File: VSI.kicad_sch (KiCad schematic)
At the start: 30 parts, among them Q1 FGH40T120SMD, Q2 FGH40T120SMD, Q3 FGH40T120SMD, Q4 FGH40T120SMD, Q5 FGH40T120SMD, Q6 FGH40T120SMD

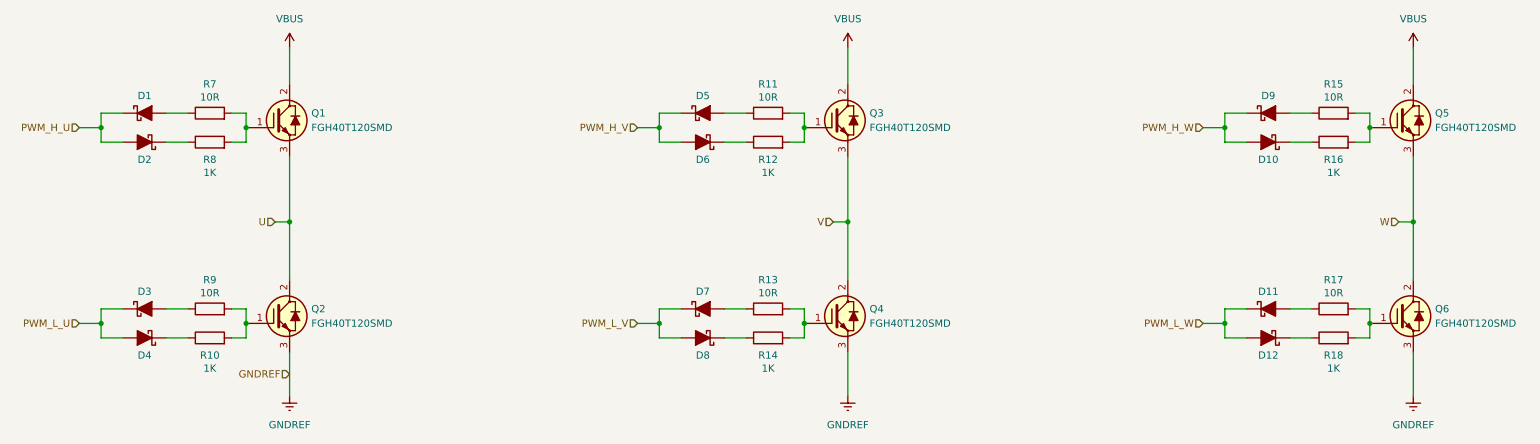
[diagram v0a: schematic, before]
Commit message: added local lib as module
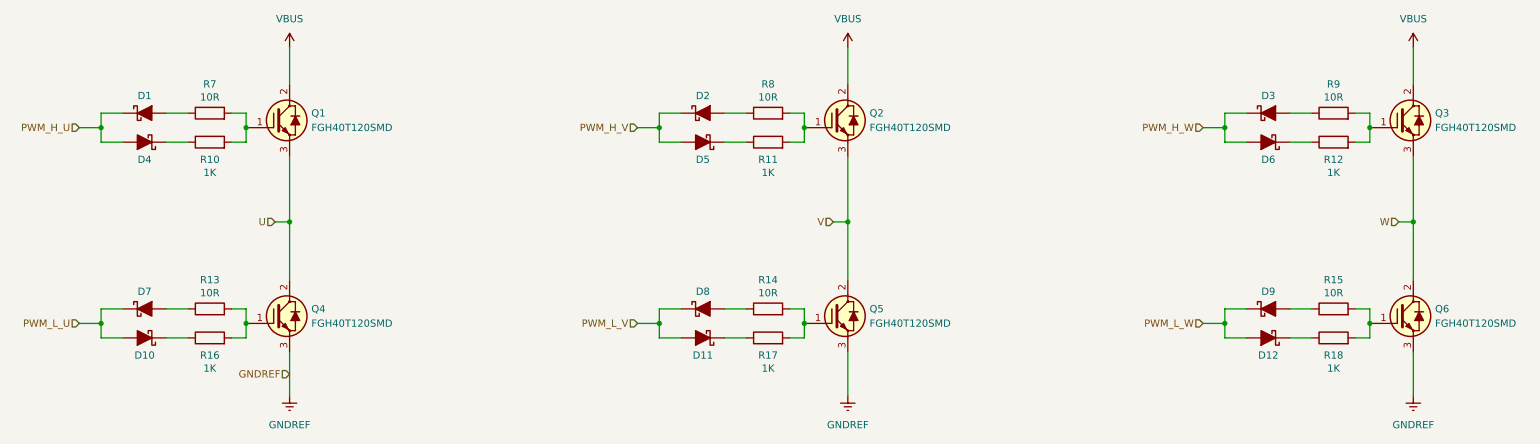
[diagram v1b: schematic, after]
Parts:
- renumbered D4 to D10, D8 to D11, D5 to D2, D9 to D3, D2 to D4, D6 to D5, D10 to D6, D3 to D7, D7 to D8, D11 to D9, Q3 to Q2, Q5 to Q3, Q2 to Q4, Q4 to Q5, R8 to R10, R12 to R11, R16 to R12, R9 to R13, R13 to R14, R17 to R15, R10 to R16, R14 to R17, R11 to R8, R15 to R9
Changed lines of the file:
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@@
 		(on_board yes)
 		(dnp no)
-		(property "Reference" "D11"
+		(property "Reference" "D9"
 			(at 236.22 112.522 0)
 			(effects
@@
 			(project "inverter"
 				(path "/6a7e1a19-486b-4340-90f8-1e7274261ff8/7fd06deb-165d-4c78-9f28-893d6b6500d1"
-					(reference "D11")
+					(reference "D9")
 					(unit 1)
 				)
@@
 		(dnp no)
 		(fields_autoplaced yes)
-		(property "Reference" "#PWR04"
+		(property "Reference" "#PWR05"
 			(at 261.62 73.66 0)
 			(effects
@@
 			(project "inverter"
 				(path "/6a7e1a19-486b-4340-90f8-1e7274261ff8/7fd06deb-165d-4c78-9f28-893d6b6500d1"
-					(reference "#PWR04")
+					(reference "#PWR05")
 					(unit 1)
 				)
@@
 		(on_board yes)
 		(dnp no)
-		(property "Reference" "R12"
+		(property "Reference" "R11"
 			(at 148.59 89.408 90)
 			(effects
@@
 			(project "inverter"
 				(path "/6a7e1a19-486b-4340-90f8-1e7274261ff8/7fd06deb-165d-4c78-9f28-893d6b6500d1"
-					(reference "R12")
+					(reference "R11")
 					(unit 1)
 				)
@@
 		(on_board yes)
 		(dnp no)
-		(property "Reference" "R10"
+		(property "Reference" "R16"
 			(at 50.8 123.698 90)
 			(effects
@@
 			(project "inverter"
 				(path "/6a7e1a19-486b-4340-90f8-1e7274261ff8/7fd06deb-165d-4c78-9f28-893d6b6500d1"
-					(reference "R10")
+					(reference "R16")
 					(unit 1)
 				)
@@
 		(dnp no)
 		(fields_autoplaced yes)
-		(property "Reference" "#PWR06"
+		(property "Reference" "#PWR07"
 			(at 162.56 137.16 0)
 			(effects
@@
 			(project "inverter"
 				(path "/6a7e1a19-486b-4340-90f8-1e7274261ff8/7fd06deb-165d-4c78-9f28-893d6b6500d1"
-					(reference "#PWR06")
+					(reference "#PWR07")
 					(unit 1)
 				)
@@
 		(on_board yes)
 		(dnp no)
-		(property "Reference" "R16"
+		(property "Reference" "R12"
 			(at 247.65 89.408 90)
 			(effects
@@
 			(project "inverter"
 				(path "/6a7e1a19-486b-4340-90f8-1e7274261ff8/7fd06deb-165d-4c78-9f28-893d6b6500d1"
-					(reference "R16")
+					(reference "R12")
 					(unit 1)
 				)
@@
 		(dnp no)
 		(fields_autoplaced yes)
-		(property "Reference" "Q5"
+		(property "Reference" "Q3"
 			(at 265.43 81.2799 0)
 			(effects
@@
 			(project "inverter"
 				(path "/6a7e1a19-486b-4340-90f8-1e7274261ff8/7fd06deb-165d-4c78-9f28-893d6b6500d1"
-					(reference "Q5")
+					(reference "Q3")
 					(unit 1)
 				)
@@
 		(dnp no)
 		(fields_autoplaced yes)
-		(property "Reference" "#PWR03"
+		(property "Reference" "#PWR04"
 			(at 162.56 73.66 0)
 			(effects
@@
 			(project "inverter"
 				(path "/6a7e1a19-486b-4340-90f8-1e7274261ff8/7fd06deb-165d-4c78-9f28-893d6b6500d1"
-					(reference "#PWR03")
+					(reference "#PWR04")
 					(unit 1)
 				)
@@
 		(on_board yes)
 		(dnp no)
-		(property "Reference" "R14"
+		(property "Reference" "R17"
 			(at 148.59 123.698 90)
 			(effects
@@
 			(project "inverter"
 				(path "/6a7e1a19-486b-4340-90f8-1e7274261ff8/7fd06deb-165d-4c78-9f28-893d6b6500d1"
-					(reference "R14")
+					(reference "R17")
 					(unit 1)
 				)
@@
 		(on_board yes)
 		(dnp no)
-		(property "Reference" "R9"
+		(property "Reference" "R13"
 			(at 50.8 110.49 90)
 			(effects
@@
 			(project "inverter"
 				(path "/6a7e1a19-486b-4340-90f8-1e7274261ff8/7fd06deb-165d-4c78-9f28-893d6b6500d1"
-					(reference "R9")
+					(reference "R13")
 					(unit 1)
 				)
@@
 		(on_board yes)
 		(dnp no)
-		(property "Reference" "D8"
+		(property "Reference" "D11"
 			(at 137.16 123.698 0)
 			(effects
@@
 			(project "inverter"
 				(path "/6a7e1a19-486b-4340-90f8-1e7274261ff8/7fd06deb-165d-4c78-9f28-893d6b6500d1"
-					(reference "D8")
+					(reference "D11")
 					(unit 1)
 				)
@@
 		(on_board yes)
 		(dnp no)
-		(property "Reference" "D6"
+		(property "Reference" "D5"
 			(at 137.16 89.408 0)
 			(effects
@@
 			(project "inverter"
 				(path "/6a7e1a19-486b-4340-90f8-1e7274261ff8/7fd06deb-165d-4c78-9f28-893d6b6500d1"
-					(reference "D6")
+					(reference "D5")
 					(unit 1)
 				)
@@
 		(dnp no)
 		(fields_autoplaced yes)
-		(property "Reference" "Q3"
+		(property "Reference" "Q2"
 			(at 166.37 81.2799 0)
 			(effects
@@
 			(project "inverter"
 				(path "/6a7e1a19-486b-4340-90f8-1e7274261ff8/7fd06deb-165d-4c78-9f28-893d6b6500d1"
-					(reference "Q3")
+					(reference "Q2")
 					(unit 1)
 				)
@@
 		(on_board yes)
 		(dnp no)
-		(property "Reference" "R17"
+		(property "Reference" "R15"
 			(at 247.65 110.49 90)
 			(effects
@@
 			(project "inverter"
 				(path "/6a7e1a19-486b-4340-90f8-1e7274261ff8/7fd06deb-165d-4c78-9f28-893d6b6500d1"
-					(reference "R17")
+					(reference "R15")
 					(unit 1)
 				)
@@
 		(on_board yes)
 		(dnp no)
-		(property "Reference" "R11"
+		(property "Reference" "R8"
 			(at 148.59 76.2 90)
 			(effects
@@
 			(project "inverter"
 				(path "/6a7e1a19-486b-4340-90f8-1e7274261ff8/7fd06deb-165d-4c78-9f28-893d6b6500d1"
-					(reference "R11")
+					(reference "R8")
 					(unit 1)
 				)
@@
 		(on_board yes)
 		(dnp no)
-		(property "Reference" "D10"
+		(property "Reference" "D6"
 			(at 236.22 89.408 0)
 			(effects
@@
 			(project "inverter"
 				(path "/6a7e1a19-486b-4340-90f8-1e7274261ff8/7fd06deb-165d-4c78-9f28-893d6b6500d1"
-					(reference "D10")
+					(reference "D6")
 					(unit 1)
 				)
@@
 		(on_board yes)
 		(dnp no)
-		(property "Reference" "D5"
+		(property "Reference" "D2"
 			(at 137.16 78.232 0)
 			(effects
@@
 			(project "inverter"
 				(path "/6a7e1a19-486b-4340-90f8-1e7274261ff8/7fd06deb-165d-4c78-9f28-893d6b6500d1"
-					(reference "D5")
+					(reference "D2")
 					(unit 1)
 				)
@@
 		(on_board yes)
 		(dnp no)
-		(property "Reference" "R15"
+		(property "Reference" "R9"
 			(at 247.65 76.2 90)
 			(effects
@@
 			(project "inverter"
 				(path "/6a7e1a19-486b-4340-90f8-1e7274261ff8/7fd06deb-165d-4c78-9f28-893d6b6500d1"
-					(reference "R15")
+					(reference "R9")
 					(unit 1)
 				)
@@
 		(on_board yes)
 		(dnp no)
-		(property "Reference" "D9"
+		(property "Reference" "D3"
 			(at 236.22 78.232 0)
 			(effects
@@
 			(project "inverter"
 				(path "/6a7e1a19-486b-4340-90f8-1e7274261ff8/7fd06deb-165d-4c78-9f28-893d6b6500d1"
-					(reference "D9")
+					(reference "D3")
 					(unit 1)
 				)
@@
 		(on_board yes)
 		(dnp no)
-		(property "Reference" "D7"
+		(property "Reference" "D8"
 			(at 137.16 112.522 0)
 			(effects
@@
 			(project "inverter"
 				(path "/6a7e1a19-486b-4340-90f8-1e7274261ff8/7fd06deb-165d-4c78-9f28-893d6b6500d1"
-					(reference "D7")
+					(reference "D8")
 					(unit 1)
 				)
@@
 		(on_board yes)
 		(dnp no)
-		(property "Reference" "D3"
+		(property "Reference" "D7"
 			(at 39.37 112.522 0)
 			(effects
@@
 			(project "inverter"
 				(path "/6a7e1a19-486b-4340-90f8-1e7274261ff8/7fd06deb-165d-4c78-9f28-893d6b6500d1"
-					(reference "D3")
+					(reference "D7")
 					(unit 1)
 				)
@@
 		(dnp no)
 		(fields_autoplaced yes)
-		(property "Reference" "#PWR02"
+		(property "Reference" "#PWR03"
 			(at 64.77 73.66 0)
 			(effects
@@
 			(project ""
 				(path "/6a7e1a19-486b-4340-90f8-1e7274261ff8/7fd06deb-165d-4c78-9f28-893d6b6500d1"
-					(reference "#PWR02")
+					(reference "#PWR03")
 					(unit 1)
 				)
@@
 		(dnp no)
 		(fields_autoplaced yes)
-		(property "Reference" "#PWR07"
+		(property "Reference" "#PWR08"
 			(at 261.62 137.16 0)
 			(effects
@@
 			(project "inverter"
 				(path "/6a7e1a19-486b-4340-90f8-1e7274261ff8/7fd06deb-165d-4c78-9f28-893d6b6500d1"
-					(reference "#PWR07")
+					(reference "#PWR08")
 					(unit 1)
 				)
@@
 		(dnp no)
 		(fields_autoplaced yes)
-		(property "Reference" "Q2"
+		(property "Reference" "Q4"
 			(at 68.58 115.5699 0)
 			(effects
@@
 			(project "inverter"
 				(path "/6a7e1a19-486b-4340-90f8-1e7274261ff8/7fd06deb-165d-4c78-9f28-893d6b6500d1"
-					(reference "Q2")
+					(reference "Q4")
 					(unit 1)
 				)
@@
 		(dnp no)
 		(fields_autoplaced yes)
-		(property "Reference" "Q4"
+		(property "Reference" "Q5"
 			(at 166.37 115.5699 0)
 			(effects
@@
 			(project "inverter"
 				(path "/6a7e1a19-486b-4340-90f8-1e7274261ff8/7fd06deb-165d-4c78-9f28-893d6b6500d1"
-					(reference "Q4")
+					(reference "Q5")
 					(unit 1)
 				)
@@
 		(on_board yes)
 		(dnp no)
-		(property "Reference" "D2"
+		(property "Reference" "D4"
 			(at 39.37 89.408 0)
 			(effects
@@
 			(project "inverter"
 				(path "/6a7e1a19-486b-4340-90f8-1e7274261ff8/7fd06deb-165d-4c78-9f28-893d6b6500d1"
-					(reference "D2")
+					(reference "D4")
 					(unit 1)
 				)
@@
 		(on_board yes)
 		(dnp no)
-		(property "Reference" "R8"
+		(property "Reference" "R10"
 			(at 50.8 89.408 90)
 			(effects
@@
 			(project "inverter"
 				(path "/6a7e1a19-486b-4340-90f8-1e7274261ff8/7fd06deb-165d-4c78-9f28-893d6b6500d1"
-					(reference "R8")
+					(reference "R10")
 					(unit 1)
 				)
@@
 		(on_board yes)
 		(dnp no)
-		(property "Reference" "R13"
+		(property "Reference" "R14"
 			(at 148.59 110.49 90)
 			(effects
@@
 			(project "inverter"
 				(path "/6a7e1a19-486b-4340-90f8-1e7274261ff8/7fd06deb-165d-4c78-9f28-893d6b6500d1"
-					(reference "R13")
+					(reference "R14")
 					(unit 1)
 				)
@@
 		(on_board yes)
 		(dnp no)
-		(property "Reference" "D4"
+		(property "Reference" "D10"
 			(at 39.37 123.698 0)
 			(effects
@@
 			(project "inverter"
 				(path "/6a7e1a19-486b-4340-90f8-1e7274261ff8/7fd06deb-165d-4c78-9f28-893d6b6500d1"
-					(reference "D4")
+					(reference "D10")
 					(unit 1)
 				)
@@
 		(dnp no)
 		(fields_autoplaced yes)
-		(property "Reference" "#PWR05"
+		(property "Reference" "#PWR06"
 			(at 64.77 137.16 0)
 			(effects
@@
 			(project ""
 				(path "/6a7e1a19-486b-4340-90f8-1e7274261ff8/7fd06deb-165d-4c78-9f28-893d6b6500d1"
-					(reference "#PWR05")
-					(unit 1)
-				)
+					(reference "#PWR06")
+					(unit 1)
+				)

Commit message: dev: added NC flags and fixed ERC warnings. Added custom design rules for PCB Design.
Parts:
- D1, D10, D11, D12, D2, D3, D4, D5, D6, D7, D8, D9: footprint (none) -> Diode_SMD:D_SOD-123
- R10, R11, R12, R13, R14, R15, R16, R17, R18, R7, R8, R9: footprint (none) -> Resistor_SMD:R_0805_2012Metric_Pad1.20x1.40mm_HandSolder
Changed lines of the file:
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@@
 			)
 		)
-		(property "Footprint" ""
+		(property "Footprint" "Diode_SMD:D_SOD-123"
 			(at 236.22 115.57 0)
 			(effects
@@
 			)
 		)
-		(property "Footprint" ""
+		(property "Footprint" "Resistor_SMD:R_0805_2012Metric_Pad1.20x1.40mm_HandSolder"
 			(at 148.59 88.138 90)
 			(effects
@@
 			)
 		)
-		(property "Footprint" ""
+		(property "Footprint" "Resistor_SMD:R_0805_2012Metric_Pad1.20x1.40mm_HandSolder"
 			(at 50.8 122.428 90)
 			(effects
@@
 			)
 		)
-		(property "Footprint" ""
+		(property "Footprint" "Resistor_SMD:R_0805_2012Metric_Pad1.20x1.40mm_HandSolder"
 			(at 247.65 88.138 90)
 			(effects
@@
 			)
 		)
-		(property "Footprint" ""
+		(property "Footprint" "Resistor_SMD:R_0805_2012Metric_Pad1.20x1.40mm_HandSolder"
 			(at 247.65 122.428 90)
 			(effects
@@
 			)
 		)
-		(property "Footprint" ""
+		(property "Footprint" "Resistor_SMD:R_0805_2012Metric_Pad1.20x1.40mm_HandSolder"
 			(at 148.59 122.428 90)
 			(effects
@@
 			)
 		)
-		(property "Footprint" ""
+		(property "Footprint" "Resistor_SMD:R_0805_2012Metric_Pad1.20x1.40mm_HandSolder"
 			(at 50.8 117.348 90)
 			(effects
@@
 			)
 		)
-		(property "Footprint" ""
+		(property "Footprint" "Diode_SMD:D_SOD-123"
 			(at 137.16 120.65 0)
 			(effects
@@
 			)
 		)
-		(property "Footprint" ""
+		(property "Footprint" "Diode_SMD:D_SOD-123"
 			(at 39.37 81.28 0)
 			(effects
@@
 			)
 		)
-		(property "Footprint" ""
+		(property "Footprint" "Resistor_SMD:R_0805_2012Metric_Pad1.20x1.40mm_HandSolder"
 			(at 50.8 83.058 90)
 			(effects
@@
 			)
 		)
-		(property "Footprint" ""
+		(property "Footprint" "Diode_SMD:D_SOD-123"
 			(at 236.22 120.65 0)
 			(effects
@@
 			)
 		)
-		(property "Footprint" ""
+		(property "Footprint" "Diode_SMD:D_SOD-123"
 			(at 137.16 86.36 0)
 			(effects
@@
 			)
 		)
-		(property "Footprint" ""
+		(property "Footprint" "Resistor_SMD:R_0805_2012Metric_Pad1.20x1.40mm_HandSolder"
 			(at 247.65 117.348 90)
 			(effects
@@
 			)
 		)
-		(property "Footprint" ""
+		(property "Footprint" "Resistor_SMD:R_0805_2012Metric_Pad1.20x1.40mm_HandSolder"
 			(at 148.59 83.058 90)
 			(effects
@@
 			)
 		)
-		(property "Footprint" ""
+		(property "Footprint" "Diode_SMD:D_SOD-123"
 			(at 236.22 86.36 0)
 			(effects
@@
 			)
 		)
-		(property "Footprint" ""
+		(property "Footprint" "Diode_SMD:D_SOD-123"
 			(at 137.16 81.28 0)
 			(effects
@@
 			)
 		)
-		(property "Footprint" ""
+		(property "Footprint" "Resistor_SMD:R_0805_2012Metric_Pad1.20x1.40mm_HandSolder"
 			(at 247.65 83.058 90)
 			(effects
@@
 			)
 		)
-		(property "Footprint" ""
+		(property "Footprint" "Diode_SMD:D_SOD-123"
 			(at 236.22 81.28 0)
 			(effects
@@
 			)
 		)
-		(property "Footprint" ""
+		(property "Footprint" "Diode_SMD:D_SOD-123"
 			(at 137.16 115.57 0)
 			(effects
@@
 			)
 		)
-		(property "Footprint" ""
+		(property "Footprint" "Diode_SMD:D_SOD-123"
 			(at 39.37 115.57 0)
 			(effects
@@
 			)
 		)
-		(property "Footprint" ""
+		(property "Footprint" "Diode_SMD:D_SOD-123"
 			(at 39.37 86.36 0)
 			(effects
@@
 			)
 		)
-		(property "Footprint" ""
+		(property "Footprint" "Resistor_SMD:R_0805_2012Metric_Pad1.20x1.40mm_HandSolder"
 			(at 50.8 88.138 90)
 			(effects
@@
 			)
 		)
-		(property "Footprint" ""
+		(property "Footprint" "Resistor_SMD:R_0805_2012Metric_Pad1.20x1.40mm_HandSolder"
 			(at 148.59 117.348 90)
 			(effects
@@
 			)
 		)
-		(property "Footprint" ""
+		(property "Footprint" "Diode_SMD:D_SOD-123"
 			(at 39.37 120.65 0)
 			(effects
